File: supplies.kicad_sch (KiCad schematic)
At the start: 32 parts, among them J10 Conn_XT_Sink, U18 LMR36520, U19 LMR36520, U20 LM7812_TO220, U25 tps3824-50

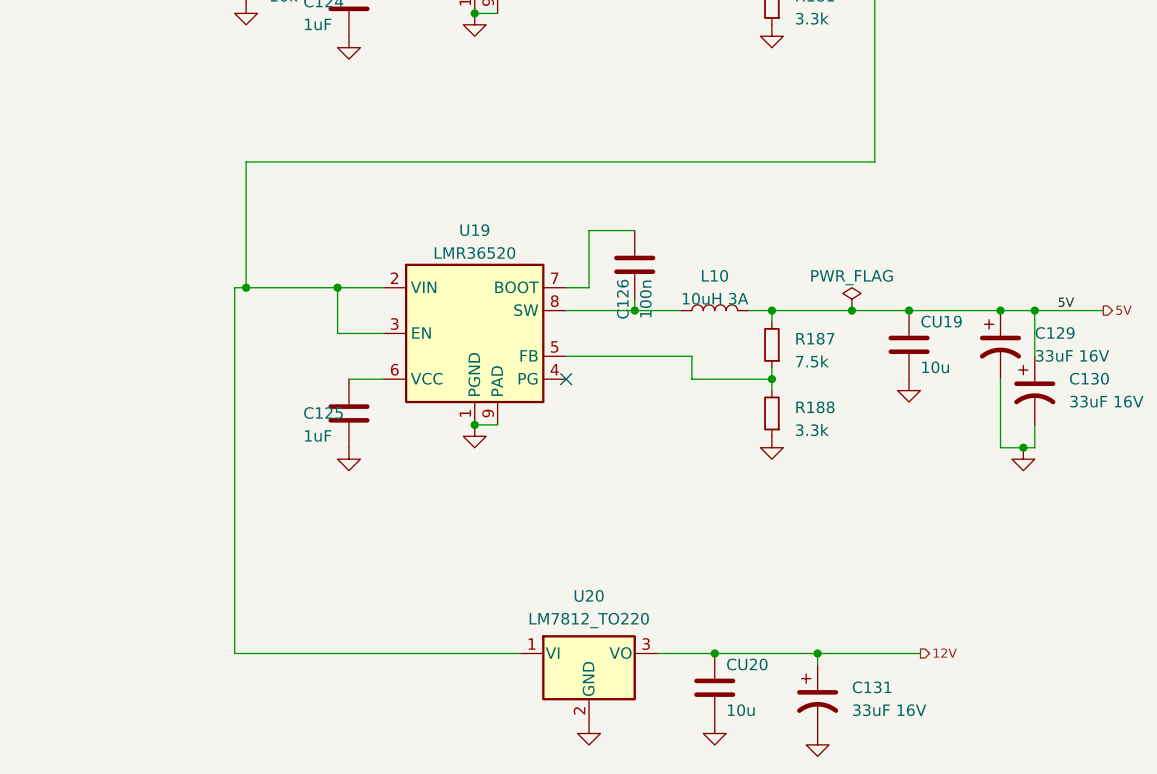
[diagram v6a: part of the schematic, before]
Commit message: routing...
+ swap around dac channels, otherwise routing was crazy
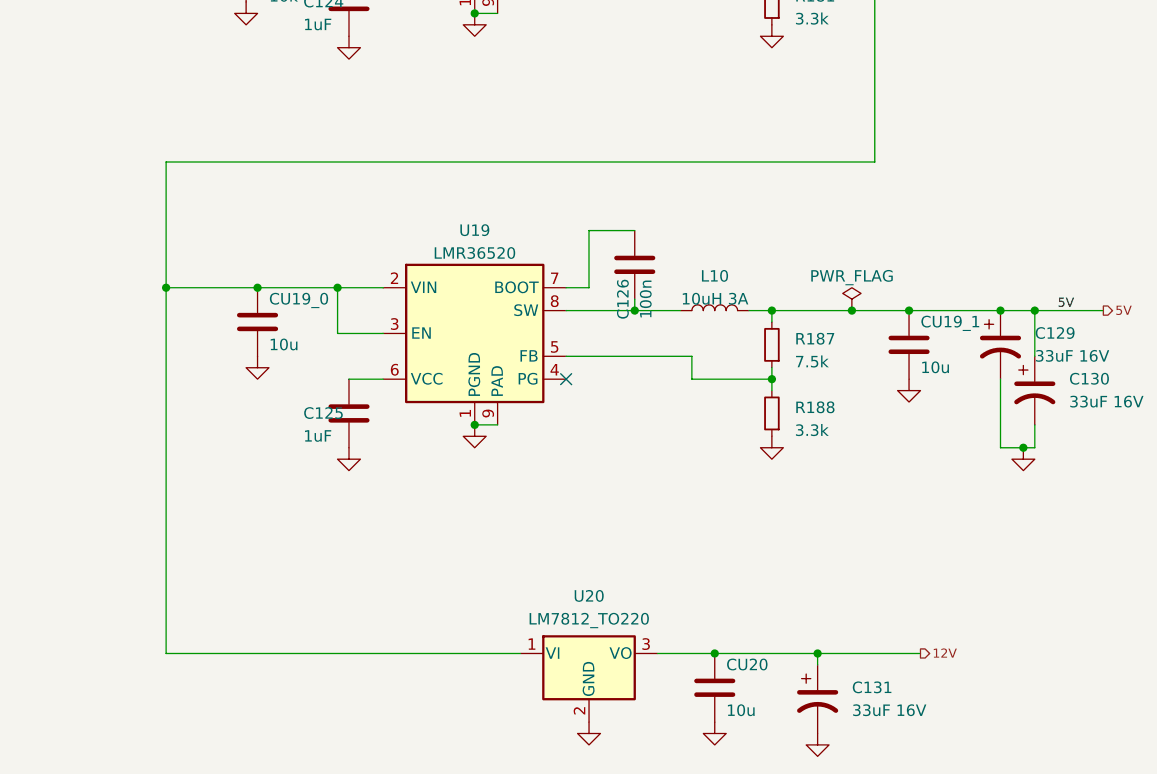
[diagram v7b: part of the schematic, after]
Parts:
- added CU19_0: 10u, invendelirium_audio:C_0603, symbol Device:C
- C127, C128, C132, C162: footprint Capacitor_THT:CP_Radial_D12.5mm_P5.00mm -> invendelirium_general:CP_Radial_D12.5mm_P5.00mm
- renumbered CU19 to CU19_1
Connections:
- net 15V: now also CU19_0.1
- net GND: now also CU19_0.2
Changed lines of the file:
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@@
 	)
 	(junction
-		(at 80.01 101.6)
+		(at 138.43 58.42)
 		(diameter 0)
 		(color 0 0 0 0)
 	)
 	(junction
-		(at 138.43 58.42)
+		(at 68.58 25.4)
 		(diameter 0)
 		(color 0 0 0 0)
 	)
 	(junction
-		(at 68.58 25.4)
+		(at 138.43 66.04)
 		(diameter 0)
 		(color 0 0 0 0)
 	)
 	(junction
-		(at 138.43 66.04)
+		(at 71.12 101.6)
 		(diameter 0)
 		(color 0 0 0 0)
@@
 	)
 	(junction
+		(at 81.28 101.6)
+		(diameter 0)
+		(color 0 0 0 0)
+	)
+	(junction
 		(at 132.08 142.24)
 		(diameter 0)
@@
 	(wire
 		(pts
-			(xy 78.74 142.24) (xy 78.74 101.6)
-		)
-		(stroke
-			(width 0)
-			(type default)
-		)
-	)
-	(wire
-		(pts
-			(xy 80.01 101.6) (xy 90.17 101.6)
+			(xy 71.12 142.24) (xy 71.12 101.6)
 		)
 		(stroke
@@
 	(wire
 		(pts
-			(xy 80.01 101.6) (xy 80.01 87.63)
+			(xy 71.12 101.6) (xy 71.12 87.63)
 		)
 		(stroke
@@
 	(wire
 		(pts
+			(xy 81.28 101.6) (xy 90.17 101.6)
+		)
+		(stroke
+			(width 0)
+			(type default)
+		)
+	)
+	(wire
+		(pts
 			(xy 115.57 101.6) (xy 118.11 101.6)
 		)
@@
 	(wire
 		(pts
-			(xy 110.49 142.24) (xy 78.74 142.24)
+			(xy 110.49 142.24) (xy 71.12 142.24)
 		)
 		(stroke
@@
 	(wire
 		(pts
-			(xy 80.01 87.63) (xy 149.86 87.63)
+			(xy 71.12 87.63) (xy 149.86 87.63)
 		)
 		(stroke
@@
 	(wire
 		(pts
-			(xy 78.74 101.6) (xy 80.01 101.6)
+			(xy 71.12 101.6) (xy 81.28 101.6)
 		)
 		(stroke
@@
 			)
 		)
-		(property "Footprint" "Capacitor_THT:CP_Radial_D12.5mm_P5.00mm"
+		(property "Footprint" "invendelirium_general:CP_Radial_D12.5mm_P5.00mm"
 			(at 49.2252 35.56 0)
 			(effects
@@
 	(symbol
 		(lib_id "power:GND")
+		(at 81.28 109.22 0)
+		(unit 1)
+		(exclude_from_sim no)
+		(in_bom yes)
+		(on_board yes)
+		(dnp no)
+		(fields_autoplaced yes)
+		(property "Reference" "#PWR0197"
+			(at 81.28 115.57 0)
+			(effects
+				(font
+					(size 1.27 1.27)
+				)
+				(hide yes)
+			)
+		)
+		(property "Value" "GND"
+			(at 81.28 114.3 0)
+			(effects
+				(font
+					(size 1.27 1.27)
+				)
+				(hide yes)
+			)
+		)
+		(property "Footprint" ""
+			(at 81.28 109.22 0)
+			(effects
+				(font
+					(size 1.27 1.27)
+				)
+				(hide yes)
+			)
+		)
+		(property "Datasheet" ""
+			(at 81.28 109.22 0)
+			(effects
+				(font
+					(size 1.27 1.27)
+				)
+				(hide yes)
+			)
+		)
+		(property "Description" ""
+			(at 81.28 109.22 0)
+			(effects
+				(font
+					(size 1.27 1.27)
+				)
+				(hide yes)
+			)
+		)
+		(pin "1"
+		)
+		(instances
+			(project "uberamp1"
+				(path "/310059c1-d84b-43e2-9c9a-0e426c534a12/4d0cf4b6-29af-402d-96b9-0bcbddb66920"
+					(reference "#PWR0197")
+					(unit 1)
+				)
+			)
+		)
+	)
+	(symbol
+		(lib_id "power:GND")
 		(at 166.37 119.38 0)
 		(unit 1)
@@
 			)
 		)
-		(property "Footprint" "Capacitor_THT:CP_Radial_D12.5mm_P5.00mm"
+		(property "Footprint" "invendelirium_general:CP_Radial_D12.5mm_P5.00mm"
 			(at 69.5452 35.56 0)
 			(effects
@@
 			)
 		)
-		(property "Footprint" "Capacitor_THT:CP_Radial_D12.5mm_P5.00mm"
+		(property "Footprint" "invendelirium_general:CP_Radial_D12.5mm_P5.00mm"
 			(at 79.7052 35.56 0)
 			(effects
@@
 		(on_board yes)
 		(dnp no)
-		(property "Reference" "CU19"
+		(property "Reference" "CU19_1"
 			(at 154.94 105.41 0)
 			(effects
@@
 			(project "uberamp1"
 				(path "/310059c1-d84b-43e2-9c9a-0e426c534a12/4d0cf4b6-29af-402d-96b9-0bcbddb66920"
-					(reference "CU19")
+					(reference "CU19_1")
+					(unit 1)
+				)
+			)
+		)
+	)
+	(symbol
+		(lib_id "Device:C")
+		(at 81.28 105.41 0)
+		(unit 1)
+		(exclude_from_sim no)
+		(in_bom yes)
+		(on_board yes)
+		(dnp no)
+		(property "Reference" "CU19_0"
+			(at 82.55 102.87 0)
+			(effects
+				(font
+					(size 1.27 1.27)
+				)
+				(justify left)
+			)
+		)
+		(property "Value" "10u"
+			(at 82.55 107.95 0)
+			(effects
+				(font
+					(size 1.27 1.27)
+				)
+				(justify left)
+			)
+		)
+		(property "Footprint" "invendelirium_audio:C_0603"
+			(at 82.2452 109.22 0)
+			(effects
+				(font
+					(size 1.27 1.27)
+				)
+				(hide yes)
+			)
+		)
+		(property "Datasheet" "~"
+			(at 81.28 105.41 0)
+			(effects
+				(font
+					(size 1.27 1.27)
+				)
+				(hide yes)
+			)
+		)
+		(property "Description" ""
+			(at 81.28 105.41 0)
+			(effects
+				(font
+					(size 1.27 1.27)
+				)
+				(hide yes)
+			)
+		)
+		(property "Voltage" "16V"
+			(at 81.28 105.41 0)
+			(effects
+				(font
+					(size 1.27 1.27)
+				)
+				(hide yes)
+			)
+		)
+		(property "Sim.Device" ""
+			(at 81.28 105.41 0)
+			(effects
+				(font
+					(size 1.27 1.27)
+				)
+				(hide yes)
+			)
+		)
+		(property "Sim.Library" ""
+			(at 81.28 105.41 0)
+			(effects
+				(font
+					(size 1.27 1.27)
+				)
+				(hide yes)
+			)
+		)
+		(property "Sim.Name" ""
+			(at 81.28 105.41 0)
+			(effects
+				(font
+					(size 1.27 1.27)
+				)
+				(hide yes)
+			)
+		)
+		(property "Sim.Pins" ""
+			(at 81.28 105.41 0)
+			(effects
+				(font
+					(size 1.27 1.27)
+				)
+				(hide yes)
+			)
+		)
+		(pin "1"
+		)
+		(pin "2"
+		)
+		(instances
+			(project "uberamp1"
+				(path "/310059c1-d84b-43e2-9c9a-0e426c534a12/4d0cf4b6-29af-402d-96b9-0bcbddb66920"
+					(reference "CU19_0")
 					(unit 1)
 				)
@@
 			)
 		)
-		(property "Footprint" "Capacitor_THT:CP_Radial_D12.5mm_P5.00mm"
+		(property "Footprint" "invendelirium_general:CP_Radial_D12.5mm_P5.00mm"
 			(at 59.3852 35.56 0)
 			(effects

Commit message: lots of drc-related work
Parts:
- J10: footprint Connector_AMASS:AMASS_XT30U-M_1x02_P5.0mm_Vertical -> invendelirium_general:AMASS_XT30U-M_1x02_P5.0mm_Vertical
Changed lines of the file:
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@@
 			)
 		)
-		(property "Footprint" "Connector_AMASS:AMASS_XT30U-M_1x02_P5.0mm_Vertical"
+		(property "Footprint" "invendelirium_general:AMASS_XT30U-M_1x02_P5.0mm_Vertical"
 			(at 24.13 30.48 0)
 			(effects
